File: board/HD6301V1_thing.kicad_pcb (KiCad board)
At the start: 2 copper layers, 99.1 x 99.1 mm, 36 parts, among them J1 Conn_01x02_Male, J2 8bit_thing_bus_connector, J3 P1_connector, J4 P2_conn, SW1 Reset, SW2 SW_DIP_x02, U1 APX811-46, U2 CD4053B, U3 HD6301V1, U4 SLG46826G, U5 74HCT573, U6 IS62C256AL, U7 SST39SF010, X1 CXO_DIP14

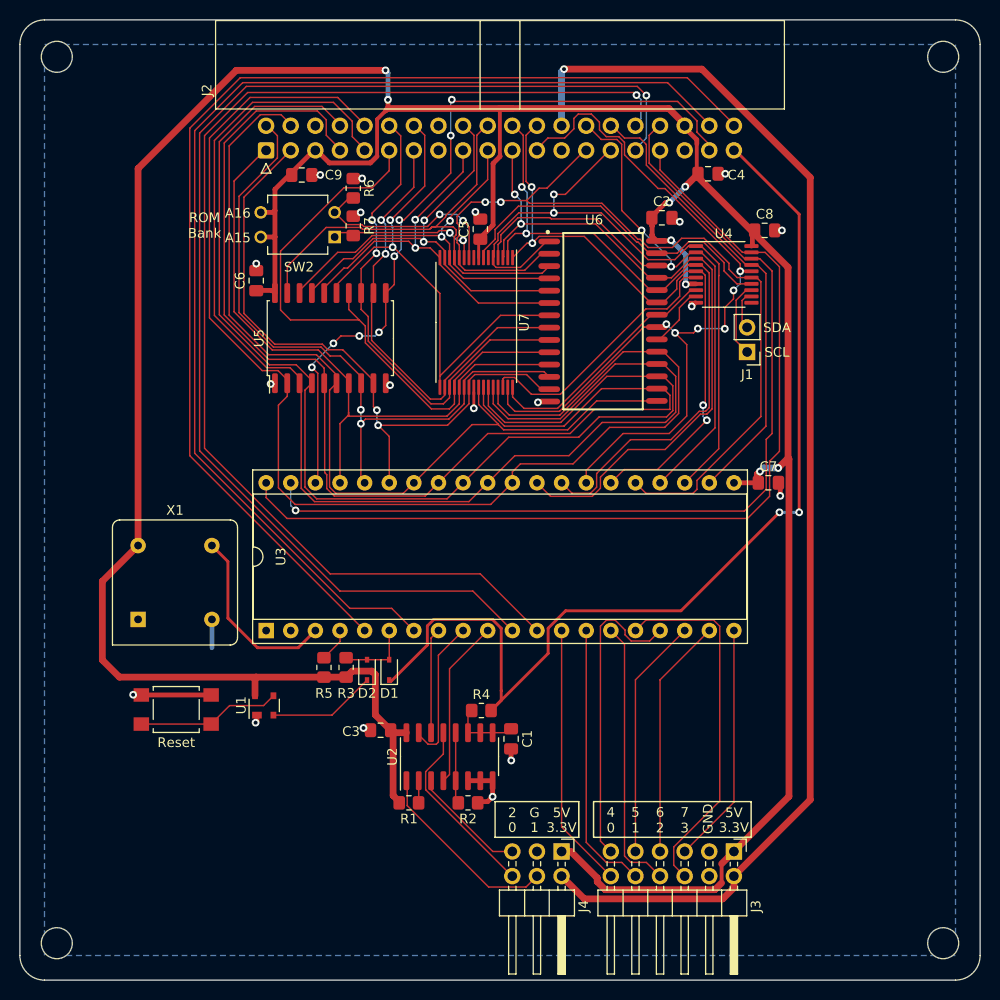
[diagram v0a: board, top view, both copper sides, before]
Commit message: Finished HD6301 board
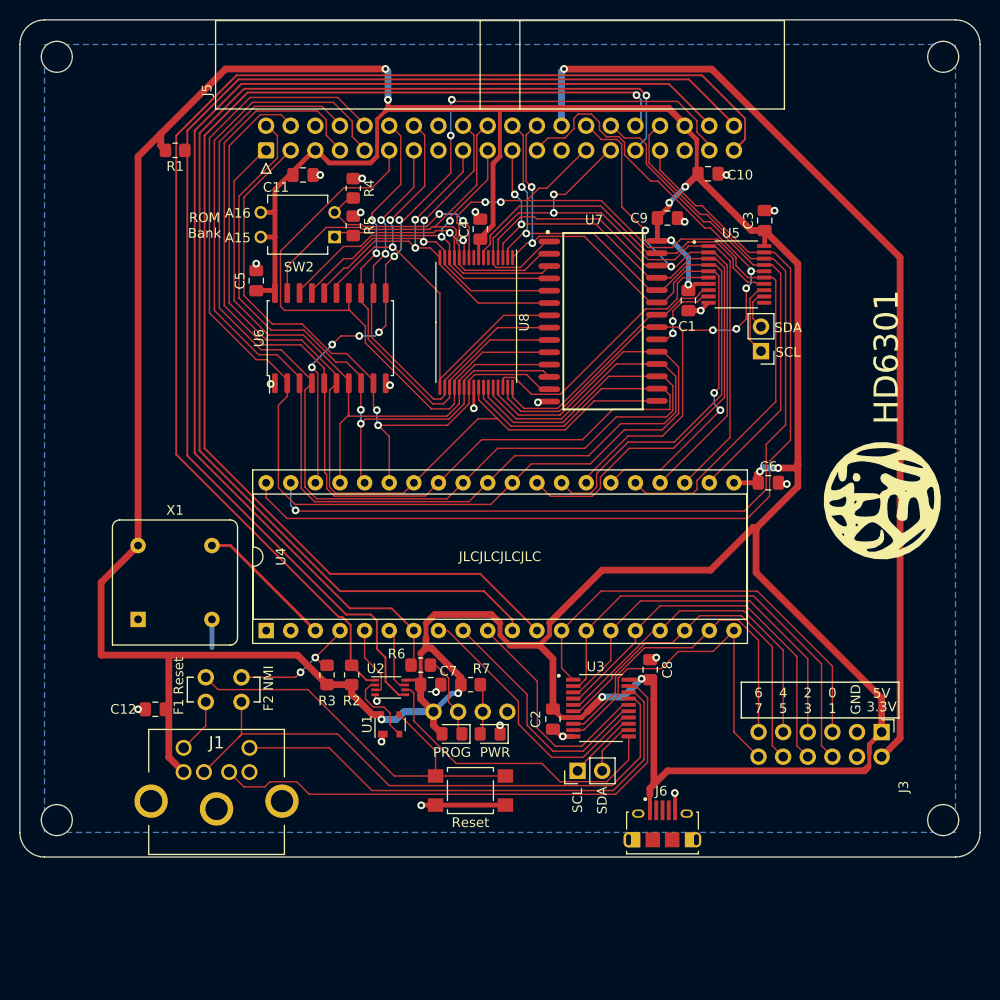
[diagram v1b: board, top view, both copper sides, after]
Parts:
- removed the C1 at (76.1, 99.6)
- removed the C3 at (62.6, 98.7)
- removed the J4 at (81.3, 111.2)
- removed the R2 at (71.6, 106.2)
- removed the R4 at (73.0, 96.6)
- added C12: 4.7u, Capacitor_SMD:C_0805_2012Metric_Pad1.18x1.45mm_HandSolder, F.Cu at (39.4, 96.5)
- added C2: 100n, Capacitor_SMD:C_0805_2012Metric_Pad1.18x1.45mm_HandSolder, F.Cu at (80.4, 97.5)
- added C7: 100n, Capacitor_SMD:C_0805_2012Metric_Pad1.18x1.45mm_HandSolder, F.Cu at (67.8, 94.0)
- added C8: 100n, Capacitor_SMD:C_0805_2012Metric_Pad1.18x1.45mm_HandSolder, F.Cu at (90.4, 92.4)
- added C9: 100n, Capacitor_SMD:C_0805_2012Metric_Pad1.18x1.45mm_HandSolder, F.Cu at (92.2, 45.8)
- added G***: LOGO, own_footprints:smyrill_logo, F.Cu at (114.3, 74.9)
- added G***: LOGO, own_footprints:smyrill_logo_small, B.Cu at (116.8, 35.6)
- added J1: KMDGX-6S-BS, imported_footprints:KMDGX6SBS, F.Cu at (47.0, 103.0)
- added J2: ps2_i2c, Connector_PinHeader_2.54mm:PinHeader_1x02_P2.54mm_Vertical, F.Cu at (82.9, 102.9)
- added J6: USB_B_Micro, imported_footprints:AMPHENOL_10118194-0001LF_MICRO_USB_improved, F.Cu at (91.7, 110.0)
- added J7: prog_LED, own_footprints:PinHeader_1x02_P2.54mm_Vertical_minimal, F.Cu at (68.1, 96.8)
- added J8: pwr_LED, own_footprints:PinHeader_1x02_P2.54mm_Vertical_minimal, F.Cu at (73.2, 96.8)
- added JP1: F1_reset, Connector_PinHeader_2.54mm:PinHeader_1x02_P2.54mm_Vertical, F.Cu at (44.6, 93.2)
- added JP2: F2_nmi, Connector_PinHeader_2.54mm:PinHeader_1x02_P2.54mm_Vertical, F.Cu at (48.3, 93.2)
- added R6: 10k, Resistor_SMD:R_0805_2012Metric_Pad1.20x1.40mm_HandSolder, F.Cu at (66.8, 92.0)
- added R7: 10k, Resistor_SMD:R_0805_2012Metric_Pad1.20x1.40mm_HandSolder, F.Cu at (71.9, 94.0)
- added U3: SLG46826G, imported_footprints:SOP65P640X120-20N, F.Cu at (85.3, 96.4)
- D1, D2: value 1N4148WS -> LED; footprint Diode_SMD:D_SOD-323 -> LED_SMD:LED_0805_2012Metric_Pad1.15x1.40mm_HandSolder
- J4: renamed from J1; value Conn_01x02_Male -> memmap_i2c
- R1: value 3.3k -> 10k
- R2: renamed from R3; value 3.3k -> 10k
- R3: renamed from R5; value 3.3k -> 10k
- SW2: value SW_DIP_x02 -> Banking
- U2: value CD4053B -> 74LVC2G08; footprint Package_SO:SOIC-16_3.9x9.9mm_P1.27mm -> Package_SO:VSSOP-8_2.3x2mm_P0.5mm
- U5: renamed from U4; footprint Package_SO:TSSOP-20_4.4x6.5mm_P0.65mm -> imported_footprints:SOP65P640X120-20N
- X1: value CXO_DIP14 -> CXO_DIP8
- moved R1 71.5 mm to (41.4, 38.9)
- moved SW1 31.5 mm to (71.9, 104.9), turned to 180 degrees
- moved J3 19.6 mm to (114.3, 98.9)
- moved D2 14.3 mm to (73.9, 99.1), turned to 180 degrees
- moved U1 13.1 mm to (63.6, 98.1)
- moved REF** 12.7 mm to (29.2, 108.0)
- moved REF** 12.7 mm to (120.7, 108.0)
- moved U2 9.41 mm to (63.6, 94.3), turned to 0 degrees
- moved D1 9.25 mm to (70.0, 99.1), turned to 180 degrees
- moved C1 8.96 mm to (94.4, 54.4), turned to -90 degrees
- moved J4 1.44 mm to (101.9, 59.6)
- moved U5 1.31 mm to (99.3, 51.7)
- moved C3 1.02 mm to (102.2, 46.1), turned to 90 degrees
- moved R2 0.97 mm to (59.6, 93.0)
- moved R3 0.84 mm to (57.1, 93.0)
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- renumbered C2 to C1, C4 to C10, C9 to C11, C8 to C3, C5 to C4, C6 to C5, C7 to C6, J2 to J5, R6 to R4, R7 to R5, U3 to U4, U5 to U6, U6 to U7, U7 to U8
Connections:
- D1 pad 1: /~{RESET} -> Net-(D1-Pad1)
- D1 pad 2: Net-(D1-Pad2) -> +5V
- D2 pad 1: Net-(D2-Pad1) -> GND
- D2 pad 2: Net-(D1-Pad2) -> Net-(D2-Pad2)
- J3 pad 10: /P11 -> /P15
- J3 pad 11: /P14 -> /P16
- J3 pad 12: /P10 -> /P17
- J3 pad 5: /P17 -> /P10
- J3 pad 6: /P13 -> /P11
- J3 pad 7: /P16 -> /P12
- J3 pad 8: /P12 -> /P13
- J3 pad 9: /P15 -> /P14
- J5 pad 39: /~{RESET} -> /~{RESET_B}
- J5 pad 40: /~{IRQ} -> /~{IRQ_B}
- R1 pad 1: Net-(R1-Pad1) -> /~{IRQ_B}
- R2 pad 1: Net-(D1-Pad2) -> /~{RESET_B}
- U1 pad 2: Net-(D2-Pad1) -> Net-(U1-Pad2)
- U2 pad 1: Net-(J4-Pad4) -> /~{RESET_B}
- U2 pad 2: Net-(R1-Pad1) -> Net-(U1-Pad2)
- U2 pad 4: /P22 -> GND
- U2 pad 5: Net-(R2-Pad2) -> /~{IRQ_B}
- U2 pad 6: GND -> Net-(U2-Pad6)
- U2 pad 7: GND -> Net-(U2-Pad7)
- U2 pad 8: GND -> +5V
- U4 pad 5: /~{IRQ} -> Net-(U2-Pad3)
- U4 pad 6: Net-(D1-Pad2) -> Net-(U2-Pad7)
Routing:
- net /~{RESET_B}: track 0.00 -> 132.1 mm
- net /~{IRQ_B}: track 0.00 -> 129.9 mm
- net /~{IRQ}: track 119.6 -> 0.00 mm
- net +5V: track 345.0 -> 454.4 mm, vias 8 -> 12
- net /~{RESET}: track 106.8 -> 0.00 mm, vias 2 -> 0
- net /~{IRQ_K}: track 0.00 -> 60.1 mm
- net /DATA_K: track 0.00 -> 55.0 mm
- net /CLK_K: track 0.00 -> 51.2 mm
- net Net-(U2-Pad6): track 0.00 -> 32.0 mm
- net +3.3V: track 132.0 -> 100.8 mm
- net Net-(JP1-Pad1): track 14.8 -> 43.0 mm
- net Net-(J4-Pad4): track 19.8 -> 0.00 mm
- net Net-(J4-Pad6): track 19.3 -> 0.00 mm
- net /P10: track 27.4 -> 45.2 mm
- net /P20: track 10.9 -> 27.5 mm
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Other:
- board size 99.1 x 99.1 mm -> 99.1 x 86.4 mm
- board text added: "0 1"
- board text added: "2 3"
- board text added: "4 5"
- board text added: "6 7"
- board text added: "F1 Reset"
- board text added: "F2 NMI"
- board text added: "HD6301"
- board text added: "HD6301 V1.0"
- board text added: "JLCJLCJLCJLC"
- board text added: "PROG"
- board text added: "PWR"
- board text removed: "0"
- board text removed: "1"
- board text removed: "2"
- board text removed: "4 0"
- board text removed: "5 1"
- board text removed: "6 2"
- board text removed: "7 3"
- board text removed: "G"

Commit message: Update board files to Kicad 7.0
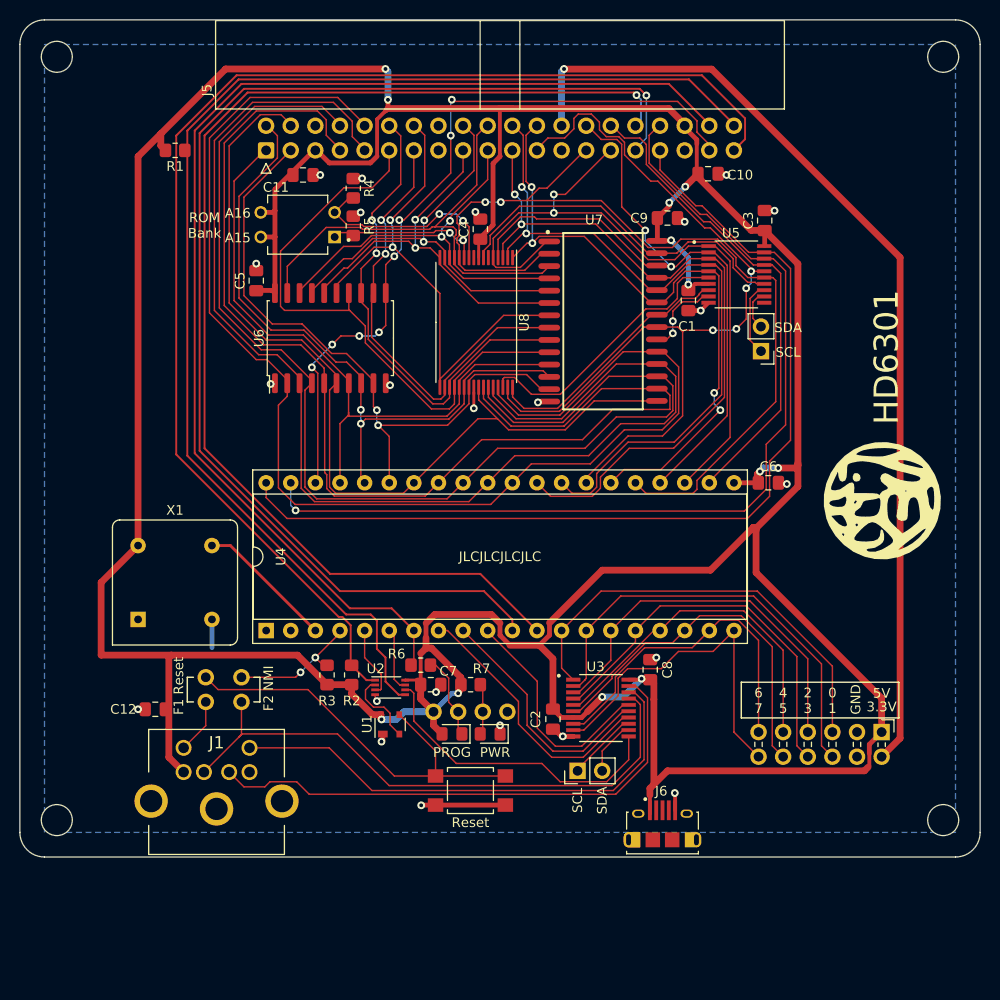
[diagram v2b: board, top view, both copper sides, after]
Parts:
- J3: footprint Connector_PinHeader_2.54mm:PinHeader_2x06_P2.54mm_Horizontal -> own_footprints:PinHeader_2x06_P2.54mm_Horizontal_no_graphics
- JP1, JP2: footprint Connector_PinHeader_2.54mm:PinHeader_1x02_P2.54mm_Vertical -> own_footprints:PinHeader_1x02_P2.54mm_Vertical_minimal

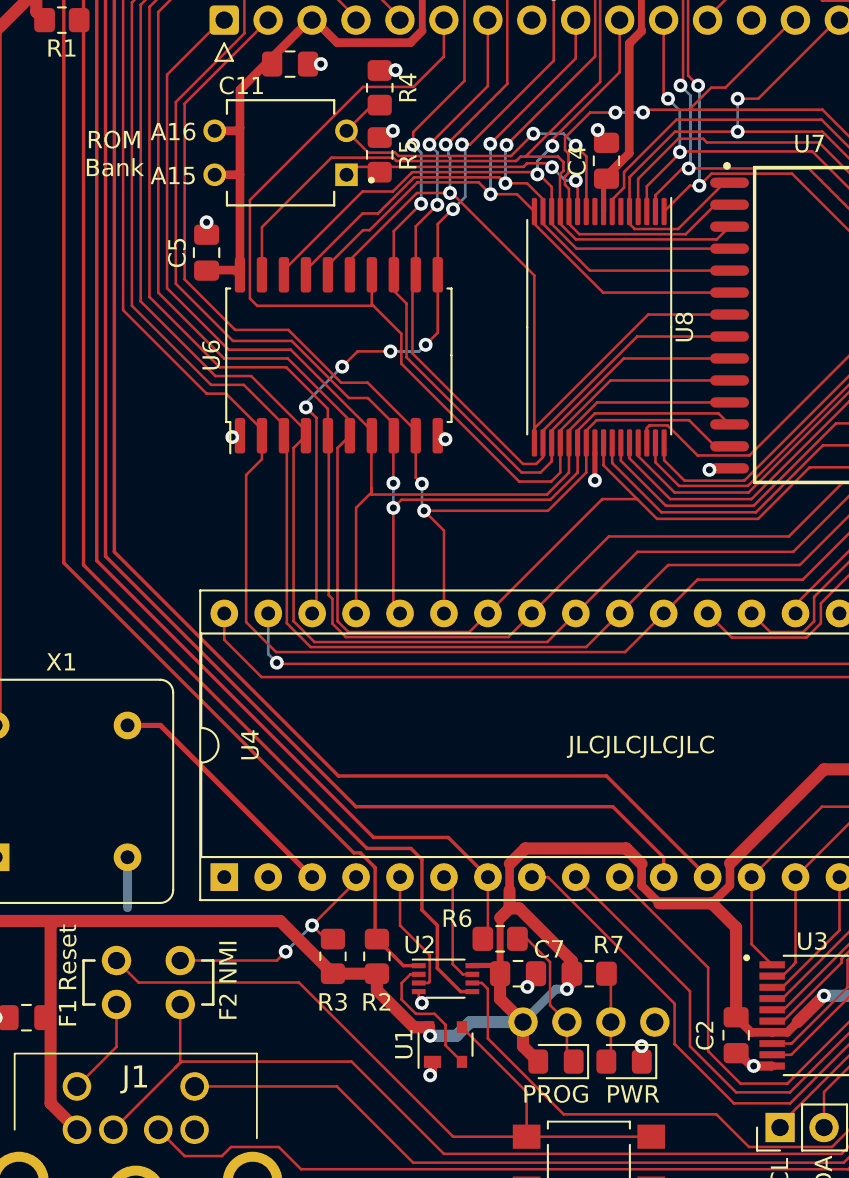
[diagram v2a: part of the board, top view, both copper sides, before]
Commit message: Update schematic for new Greenpak symbol and some small changes to the PCB
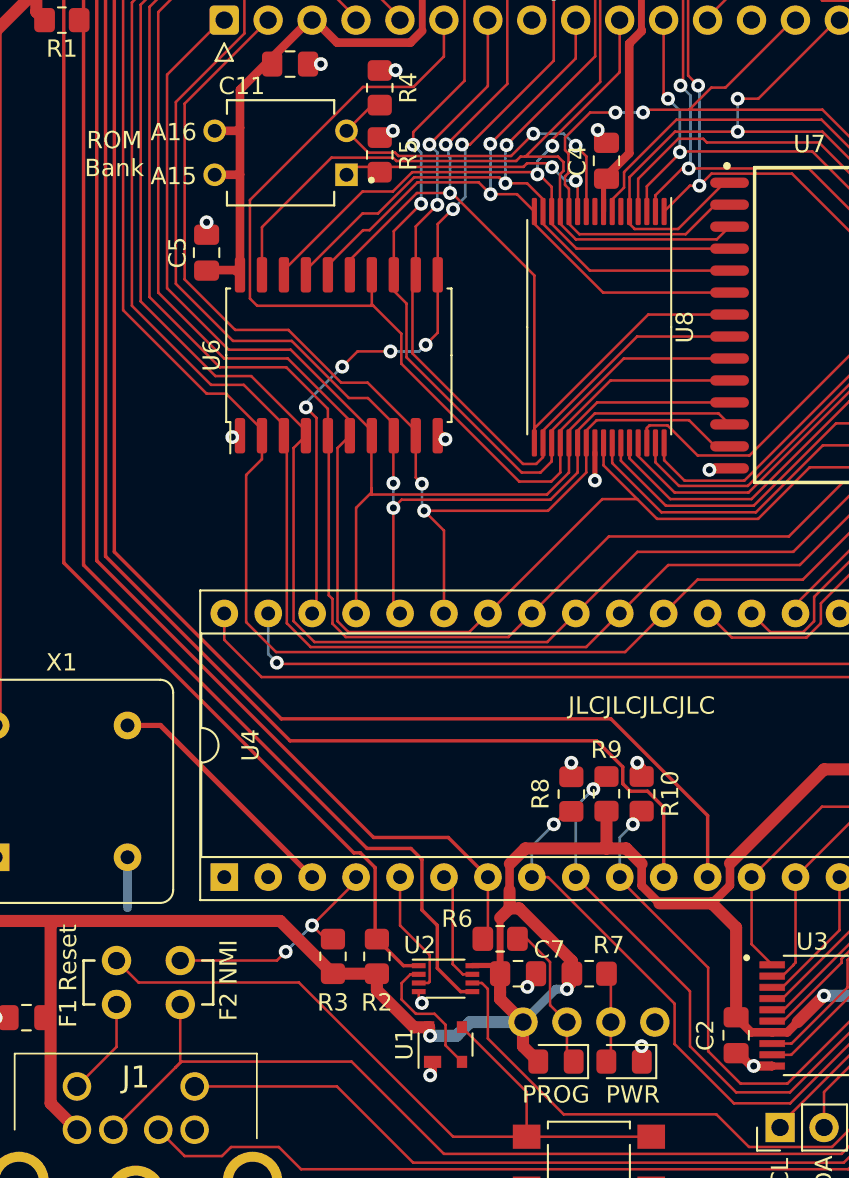
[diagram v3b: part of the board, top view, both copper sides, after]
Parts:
- added R10: 10k, Resistor_SMD:R_0805_2012Metric_Pad1.20x1.40mm_HandSolder, F.Cu at (74.9, 83.6)
- added R8: 10k, Resistor_SMD:R_0805_2012Metric_Pad1.20x1.40mm_HandSolder, F.Cu at (70.9, 83.6)
- added R9: 10k, Resistor_SMD:R_0805_2012Metric_Pad1.20x1.40mm_HandSolder, F.Cu at (72.9, 83.6)
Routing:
- net /P21: track 25.2 -> 31.8 mm, vias 0 -> 1
- net /P20: track 27.5 -> 32.2 mm, vias 0 -> 1
- net /P22: track 23.4 -> 26.8 mm, vias 0 -> 1
- net /RX: track 127.8 -> 130.0 mm
- net +5V: track 454.4 -> 456.6 mm
- net /TX: track 124.3 -> 126.4 mm
- net GND: track 35.2 -> 36.7 mm, vias 23 -> 25
- net Net-(D1-K): track 8.76 -> 8.21 mm

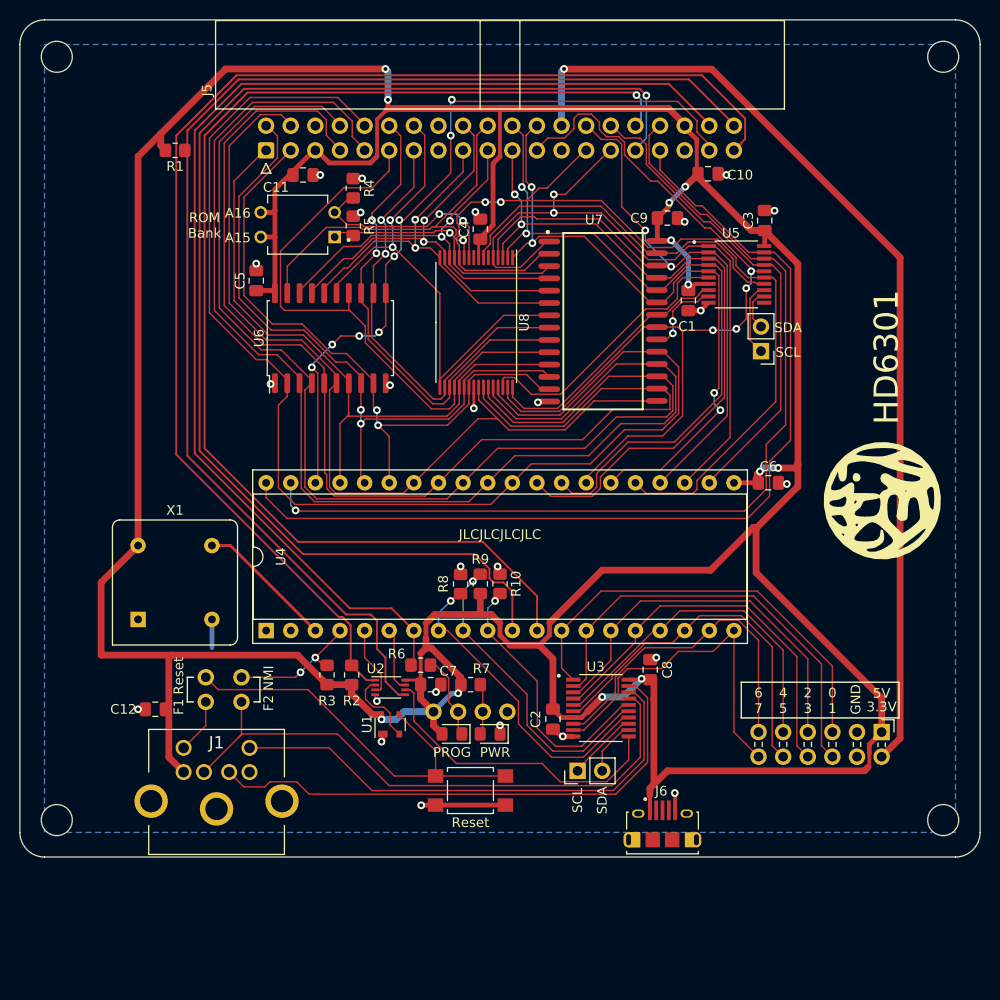
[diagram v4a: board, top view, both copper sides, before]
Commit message: Replace IRQ/RESET AND IC with a Schmitt-trigger one
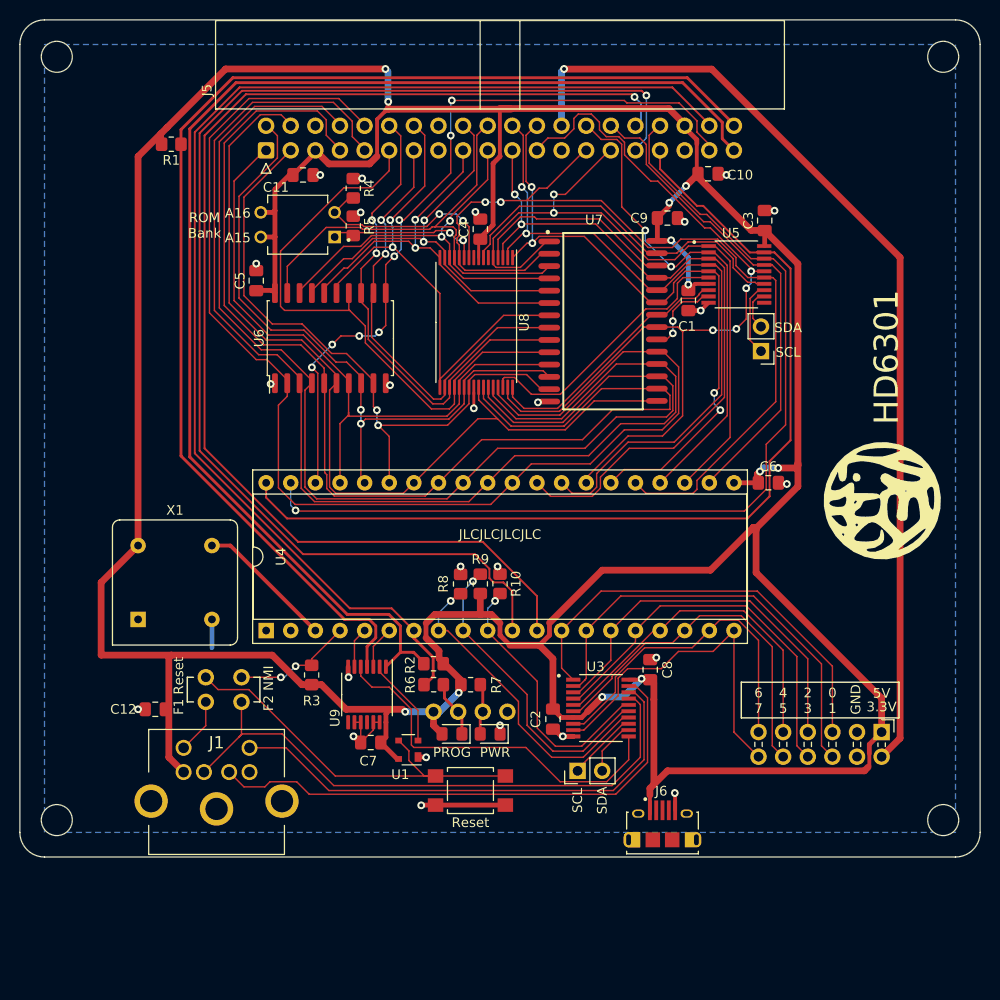
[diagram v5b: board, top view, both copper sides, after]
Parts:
- removed U2: 74LVC2G08, Package_SO:VSSOP-8_2.3x2mm_P0.5mm
- added U9: 74HCS08, Package_SO:TSSOP-14_4.4x5mm_P0.65mm, F.Cu at (61.2, 95.0)
- R1: value 10k -> 3.3k
- moved C7 8.60 mm to (61.6, 99.9), turned to 180 degrees
- moved R2 8.52 mm to (68.1, 91.8), turned to 0 degrees
- moved U1 3.22 mm to (65.5, 100.7), turned to 180 degrees
- moved R6 2.42 mm to (68.1, 94.0)
- moved R3 1.59 mm to (55.5, 93.0)
- moved R1 0.75 mm to (41.0, 38.2)
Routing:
- net Net-(U3-O6): track 32.0 -> 38.6 mm
- net GND: track 36.7 -> 43.3 mm
- net +5V: track 456.6 -> 452.3 mm
- net /~{STBY}: track 123.3 -> 126.6 mm
- net Net-(U4-~{IRQ1}): track 7.41 -> 4.17 mm
- net /~{IRQ_B}: track 129.9 -> 126.9 mm
- net Net-(D1-K): track 8.21 -> 5.28 mm
- net Net-(JP1-A): track 43.0 -> 41.0 mm
- net Net-(U4-~{RES}): track 5.91 -> 4.42 mm
- net Net-(U1-~{RESET}): track 7.83 -> 8.72 mm
- net Net-(JP2-A): track 13.2 -> 12.5 mm
- net /~{RESET_B}: track 132.1 -> 132.6 mm
